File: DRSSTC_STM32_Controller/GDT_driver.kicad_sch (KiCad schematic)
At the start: 36 parts, among them IC1 UCC27282DR, IC2 UCC27282DR, J5 Screw_Terminal_01x02, Q1 QM6006D, Q2 QM6006D, Q3 QM6006D, Q4 QM6006D

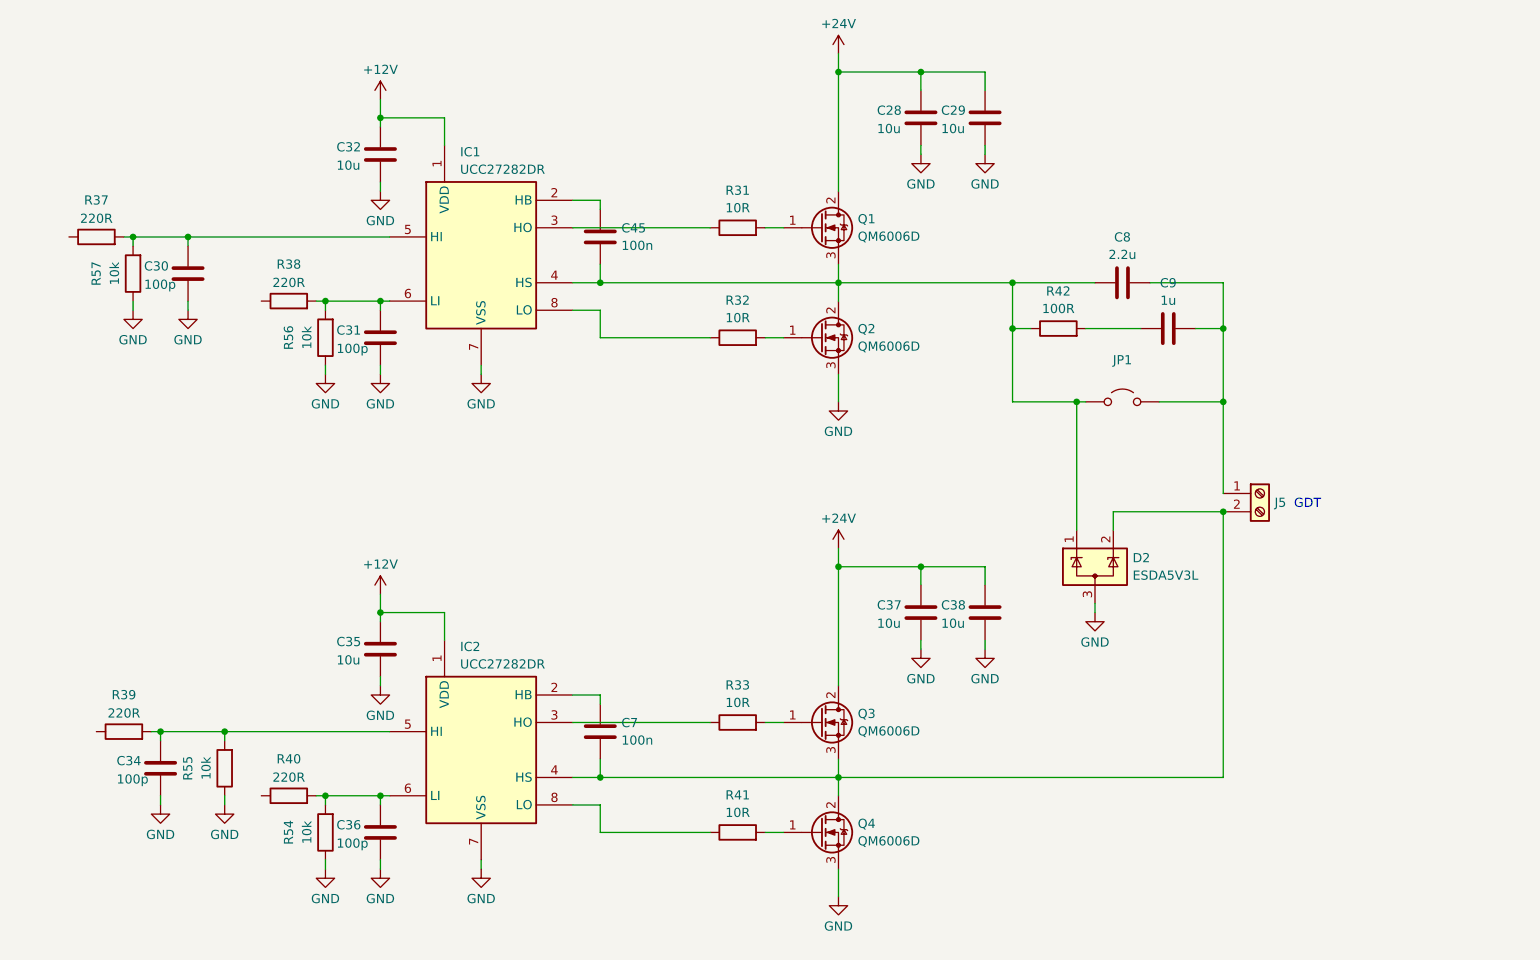
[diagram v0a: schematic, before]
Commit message: update the feedback stage simulation & controller schematic
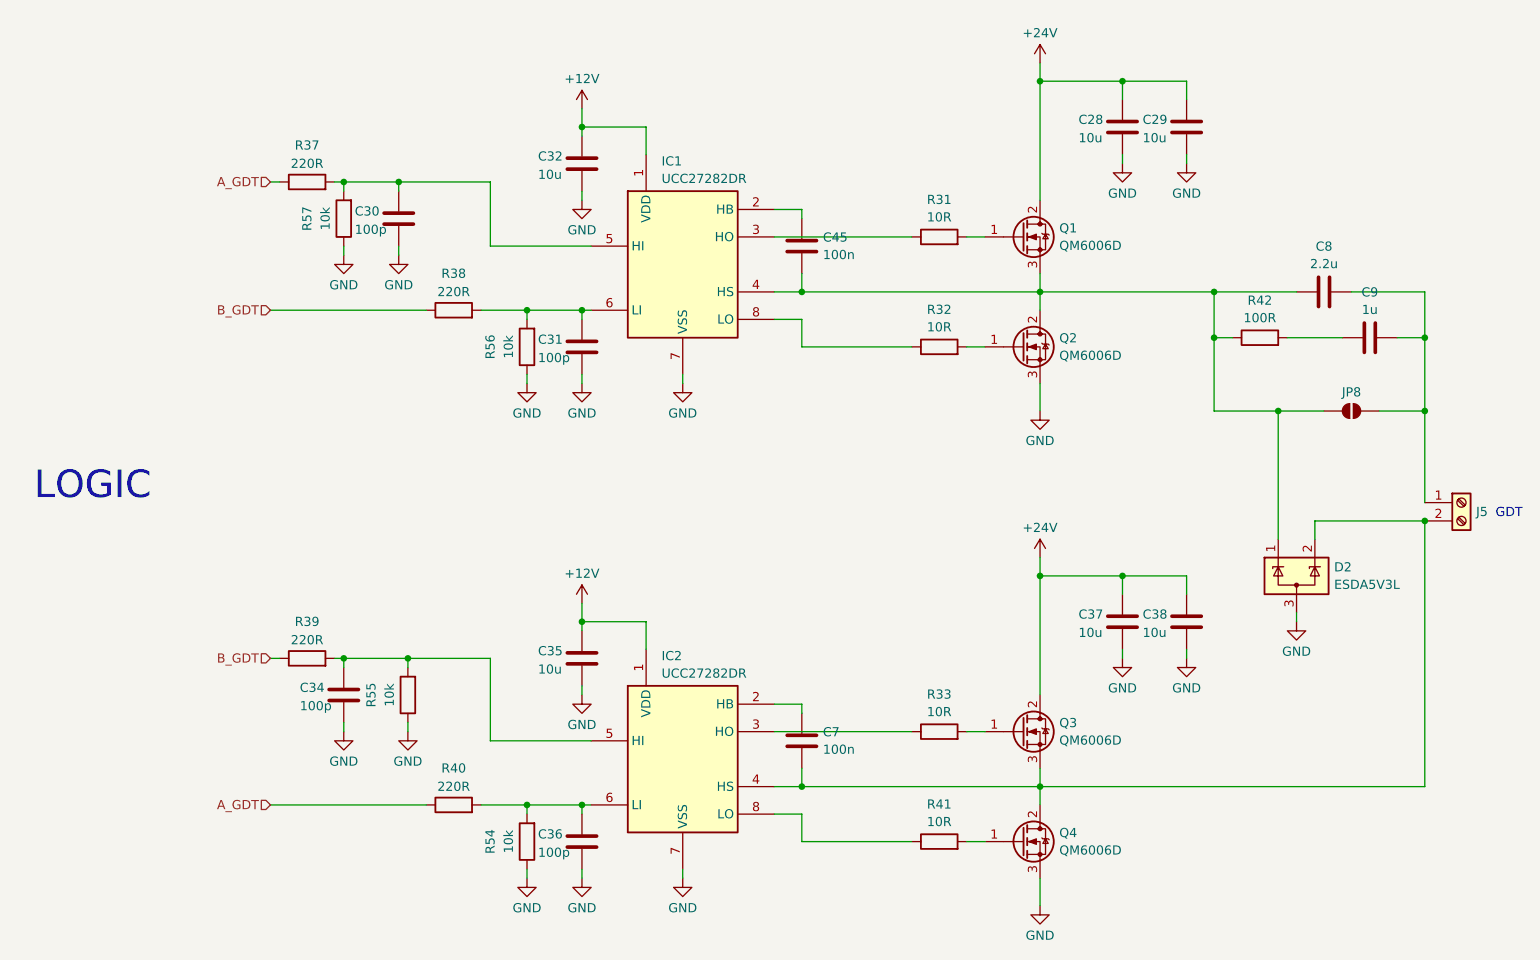
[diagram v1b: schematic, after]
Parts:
- removed JP1: Jumper_2_Open, symbol Jumper:Jumper_2_Open
- added JP8: SolderJumper_2_Open, Jumper:SolderJumper-2_P1.3mm_Open_RoundedPad1.0x1.5mm, symbol Jumper:SolderJumper_2_Open
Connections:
- net at C45.2, C8.1, D2.1 (K)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: now also JP8.2 (B)
- net at C8.2, C9.2, J5.1 (Pin_1): now also JP8.1 (A)
- net B_GDT: now reaches R38.1
- net B_GDT: now also R39.1
- net A_GDT: now reaches R37.1
- net A_GDT: now also R40.1
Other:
- note added: "LOGIC"
- moved on the sheet: C28, C29, C30, C31, C32, C34, C35, C36, C37, C38, C45, C7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

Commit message: update conroller schematics
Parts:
- removed C30, C31, C34, C36: 100p, Capacitor_SMD:C_0805_2012Metric, symbol Device:C
- removed J5: Screw_Terminal_01x02, TerminalBlock_Altech:Altech_AK100_1x02_P5.00mm, symbol Connector:Screw_Terminal_01x02
- removed R37, R38, R39, R40: 220R, Resistor_SMD:R_0805_2012Metric, symbol Device:R
- removed R54, R55, R56, R57: 10k, Resistor_SMD:R_0805_2012Metric, symbol Device:R
- added C64, C66, C70, C71, C72, C73: 10u, Capacitor_SMD:C_0805_2012Metric, symbol Device:C
- added C67, C79, C80: 1u, Capacitor_SMD:C_0805_2012Metric, symbol Device:C
- added C68, C69: 100n, symbol Device:C
- added C74: 2.2u, symbol Device:C
- added C75: 1u, symbol Device:C
- added D3: ESDA5V3L, Package_TO_SOT_SMD:SOT-23-3, symbol Power_Protection:ESDA5V3L
- added IC3, IC4: UCC27282DR, SOIC127P600X175-8N, symbol UCC27282DR:UCC27282DR
- added IC5: SN74LVC14ADR, Library:SOIC127P600X175-14N, symbol SN74LVC14ADR:SN74LVC14ADR
- added IC6, IC7: SN74LVC11ADR, Library:SOIC127P600X175-14N, symbol Library:SN74LVC11ADR
- added JP9: SolderJumper_2_Open, Jumper:SolderJumper-2_P1.3mm_Open_RoundedPad1.0x1.5mm, symbol Jumper:SolderJumper_2_Open
- added Q15, Q16, Q17, Q18: QM6006D, Package_TO_SOT_SMD:TO-252-2, symbol Transistor_FET:QM6006D
- added R119, R120, R121, R126, R139: 100R, Resistor_SMD:R_0805_2012Metric, symbol Device:R
- added R123, R124, R125, R35: 10R, Resistor_SMD:R_0805_2012Metric, symbol Device:R
- added R133, R134, R135, R136: 10k, Resistor_SMD:R_0805_2012Metric, symbol Device:R
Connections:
- net +12V: now also C64.1, C66.1, IC3.1 (VDD), IC4.1 (VDD)
- net +24V: now also C70.1, C71.1, C72.1, C73.1, Q15.2 (D), Q17.2 (D)
- net GND: now also C64.2, C66.2, C67.2, C70.2, C71.2, C72.2, C73.2, C79.2, C80.2, D3.3 (A), IC3.7 (VSS), IC4.7 (VSS), IC5.10 (5Y), IC5.11 (5A), IC5.12 (6Y), IC5.13 (6A), IC5.7 (GND), IC6.7 (GND), IC7.7 (GND), Q16.3 (S), Q18.3 (S), R133.1, R134.1, R135.1, R136.1
- net GDT1+: now reaches C8.2, C9.2, JP8.1 (A)
- net GDT1-: now reaches C7.2, D2.2 (K), IC2.4 (HS), Q3.3 (S), Q4.2 (D)
- net at IC1.6 (LI): now also IC2.5 (HI), R119.1
- net at IC1.5 (HI): now also IC2.6 (LI), R121.1
- new net: IC4.3 (HO), R124.1
- new net: Q17.1 (G), R124.2
- new net: C68.2, C74.1, D3.1 (K), IC3.4 (HS), JP9.2 (B), Q15.3 (S), Q16.2 (D), R126.1
- new net: C68.1, IC3.2 (HB)
- new net: IC3.3 (HO), R35.1
- new net: IC3.5 (HI), IC4.6 (LI), R139.2
- new net: IC3.6 (LI), IC4.5 (HI), R120.1
- new net: IC3.8 (LO), R123.1
- new net: Q18.1 (G), R125.2
- new net: IC4.8 (LO), R125.1
- new net: IC5.2 (1Y), IC6.10 (3B), IC7.5 (2C)
- new net: IC5.4 (2Y), IC6.4 (2B), IC7.9 (3A)
- new net: IC5.6 (3Y), IC6.5 (2C), IC7.10 (3B)
- new net: IC5.8 (4Y), IC6.9 (3A), IC7.4 (2B)
- new net: IC6.6 (2Y), R121.2
- new net: Q15.1 (G), R35.2
- new net: IC6.8 (3Y), R119.2
- new net: IC7.8 (3Y), R120.2
- new net: C75.1, R126.2
- new net: Q16.1 (G), R123.2
- new net: C69.1, IC4.2 (HB)
- new net: IC7.6 (2Y), R139.1
- new net +3V3: C67.1, C79.1, C80.1, IC5.14 (VCC), IC6.14 (VCC), IC7.14 (VCC)
- new net G1+: IC5.1 (1A), IC6.3 (2A), R135.2
- new net G1-: IC5.3 (2A), IC6.11 (3C), R134.2
- new net G2+: IC5.5 (3A), IC7.3 (2A), R133.2
- new net G2-: IC5.9 (4A), IC7.11 (3C), R136.2
- new net GDT2+: C74.2, C75.2, JP9.1 (A)
- new net GDT2-: C69.2, D3.2 (K), IC4.4 (HS), Q17.3 (S), Q18.2 (D)
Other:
- note added: "+"
- note added: "Hardware interlock logic"
- note added: "bridge turned off while not operationg so no dc block needed"
- note added: "deadtime in software"
- note removed: "GDT"
- note removed: "LOGIC"
- moved on the sheet: C28, C29, C32, C35, C37, C38, C45, C7, C8, C9, D2, IC1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

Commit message: assign footprints
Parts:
- C45, C68, C69: footprint (none) -> Capacitor_SMD:C_0603_1608Metric
- C67, C79, C80: footprint Capacitor_SMD:C_0805_2012Metric -> Capacitor_SMD:C_0603_1608Metric
- C7: footprint (none) -> Capacitor_SMD:C_0201_0603Metric
- C74, C75, C8, C9: footprint (none) -> Capacitor_THT:C_Axial_L12.0mm_D7.5mm_P15.00mm_Horizontal
- IC1, IC2, IC3, IC4: footprint SOIC127P600X175-8N -> Library:SOIC127P600X175-8N
- R119, R120, R121, R133, R134, R135, R136, R139: footprint Resistor_SMD:R_0805_2012Metric -> Resistor_SMD:R_0603_1608Metric
- R126, R42: footprint Resistor_SMD:R_0805_2012Metric -> Resistor_THT:R_Axial_DIN0309_L9.0mm_D3.2mm_P12.70mm_Horizontal
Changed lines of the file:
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@@
 			)
 		)
-		(property "Footprint" ""
+		(property "Footprint" "Capacitor_THT:C_Axial_L12.0mm_D7.5mm_P15.00mm_Horizontal"
 			(at 261.62 120.9548 0)
 			(hide yes)
@@
 			)
 		)
-		(property "Footprint" "SOIC127P600X175-8N"
+		(property "Footprint" "Library:SOIC127P600X175-8N"
 			(at 171.45 210.49 0)
 			(hide yes)
@@
 			)
 		)
-		(property "Footprint" "Resistor_SMD:R_0805_2012Metric"
+		(property "Footprint" "Resistor_THT:R_Axial_DIN0309_L9.0mm_D3.2mm_P12.70mm_Horizontal"
 			(at 251.46 130.048 90)
 			(hide yes)
@@
 			)
 		)
-		(property "Footprint" "Resistor_SMD:R_0805_2012Metric"
+		(property "Footprint" "Resistor_SMD:R_0603_1608Metric"
 			(at 112.268 149.86 90)
 			(hide yes)
@@
 			)
 		)
-		(property "Footprint" "Capacitor_SMD:C_0805_2012Metric"
+		(property "Footprint" "Capacitor_SMD:C_0603_1608Metric"
 			(at 108.9152 132.08 0)
 			(hide yes)
@@
 			)
 		)
-		(property "Footprint" "SOIC127P600X175-8N"
+		(property "Footprint" "Library:SOIC127P600X175-8N"
 			(at 170.18 356.54 0)
 			(hide yes)
@@
 			)
 		)
-		(property "Footprint" "Resistor_SMD:R_0805_2012Metric"
+		(property "Footprint" "Resistor_SMD:R_0603_1608Metric"
 			(at 37.338 147.32 90)
 			(hide yes)
@@
 			)
 		)
-		(property "Footprint" "SOIC127P600X175-8N"
+		(property "Footprint" "Library:SOIC127P600X175-8N"
 			(at 171.45 279.07 0)
 			(hide yes)
@@
 			)
 		)
-		(property "Footprint" "Capacitor_SMD:C_0805_2012Metric"
+		(property "Footprint" "Capacitor_SMD:C_0603_1608Metric"
 			(at 102.5652 205.74 0)
 			(hide yes)
@@
 			)
 		)
-		(property "Footprint" "Resistor_SMD:R_0805_2012Metric"
+		(property "Footprint" "Resistor_SMD:R_0603_1608Metric"
 			(at 29.718 147.32 90)
 			(hide yes)
@@
 			)
 		)
-		(property "Footprint" "Resistor_SMD:R_0805_2012Metric"
+		(property "Footprint" "Resistor_SMD:R_0603_1608Metric"
 			(at 118.872 234.95 90)
 			(hide yes)
@@
 			)
 		)
-		(property "Footprint" "Resistor_SMD:R_0805_2012Metric"
+		(property "Footprint" "Resistor_SMD:R_0603_1608Metric"
 			(at 44.958 147.32 90)
 			(hide yes)
@@
 			)
 		)
-		(property "Footprint" "Resistor_SMD:R_0805_2012Metric"
+		(property "Footprint" "Resistor_SMD:R_0603_1608Metric"
 			(at 115.062 295.91 90)
 			(hide yes)
@@
 			)
 		)
-		(property "Footprint" ""
+		(property "Footprint" "Capacitor_THT:C_Axial_L12.0mm_D7.5mm_P15.00mm_Horizontal"
 			(at 260.35 265.7348 0)
 			(hide yes)
@@
 			)
 		)
-		(property "Footprint" "Resistor_SMD:R_0805_2012Metric"
+		(property "Footprint" "Resistor_SMD:R_0603_1608Metric"
 			(at 121.412 191.77 90)
 			(hide yes)
@@
 			)
 		)
-		(property "Footprint" ""
+		(property "Footprint" "Capacitor_THT:C_Axial_L12.0mm_D7.5mm_P15.00mm_Horizontal"
 			(at 265.43 272.0848 0)
 			(hide yes)
@@
 			)
 		)
-		(property "Footprint" ""
+		(property "Footprint" "Capacitor_SMD:C_0603_1608Metric"
 			(at 178.7652 264.16 0)
 			(hide yes)
@@
 			)
 		)
-		(property "Footprint" "Capacitor_SMD:C_0805_2012Metric"
+		(property "Footprint" "Capacitor_SMD:C_0603_1608Metric"
 			(at 96.2152 308.61 0)
 			(hide yes)
@@
 			)
 		)
-		(property "Footprint" ""
+		(property "Footprint" "Capacitor_SMD:C_0201_0603Metric"
 			(at 180.0352 186.69 0)
 			(hide yes)
@@
 			)
 		)
-		(property "Footprint" "SOIC127P600X175-8N"
+		(property "Footprint" "Library:SOIC127P600X175-8N"
 			(at 170.18 425.12 0)
 			(hide yes)
@@
 			)
 		)
-		(property "Footprint" ""
+		(property "Footprint" "Capacitor_THT:C_Axial_L12.0mm_D7.5mm_P15.00mm_Horizontal"
 			(at 267.97 127.3048 0)
 			(hide yes)
@@
 			)
 		)
-		(property "Footprint" ""
+		(property "Footprint" "Capacitor_SMD:C_0603_1608Metric"
 			(at 180.0352 118.11 0)
 			(hide yes)
@@
 			)
 		)
-		(property "Footprint" "Resistor_SMD:R_0805_2012Metric"
+		(property "Footprint" "Resistor_SMD:R_0603_1608Metric"
 			(at 121.92 339.598 90)
 			(hide yes)
@@
 			)
 		)
-		(property "Footprint" ""
+		(property "Footprint" "Capacitor_SMD:C_0603_1608Metric"
 			(at 178.7652 332.74 0)
 			(hide yes)
@@
 			)
 		)
-		(property "Footprint" "Resistor_SMD:R_0805_2012Metric"
+		(property "Footprint" "Resistor_THT:R_Axial_DIN0309_L9.0mm_D3.2mm_P12.70mm_Horizontal"
 			(at 250.19 274.828 90)
 			(hide yes)

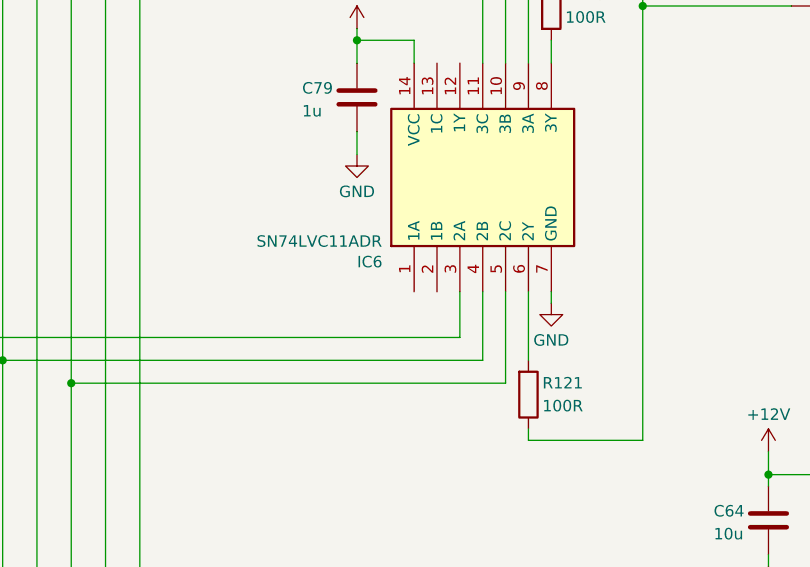
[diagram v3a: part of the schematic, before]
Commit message: start cintrollenr routing
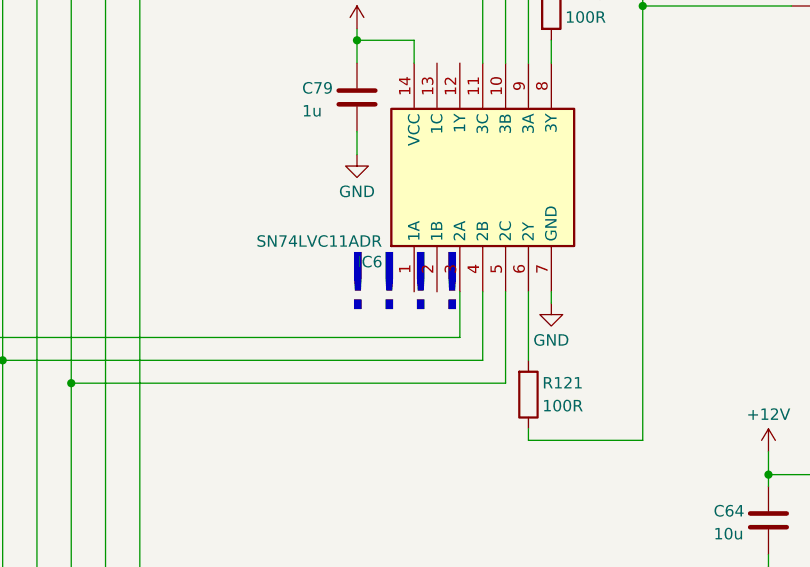
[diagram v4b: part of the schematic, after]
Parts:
- C7: footprint Capacitor_SMD:C_0201_0603Metric -> Capacitor_SMD:C_0603_1608Metric
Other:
- note added: "!!!!"
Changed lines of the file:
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@@
 		)
 	)
+	(text "!!!!"
+		(exclude_from_sim no)
+		(at 106.934 222.758 0)
+		(effects
+			(font
+				(size 6.35 6.35)
+			)
+		)
+	)
 	(text "+"
 		(exclude_from_sim no)
@@
 			)
 		)
-		(property "Footprint" "Capacitor_SMD:C_0201_0603Metric"
+		(property "Footprint" "Capacitor_SMD:C_0603_1608Metric"
 			(at 180.0352 186.69 0)
 			(hide yes)
